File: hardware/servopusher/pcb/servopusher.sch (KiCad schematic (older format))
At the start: 1 part

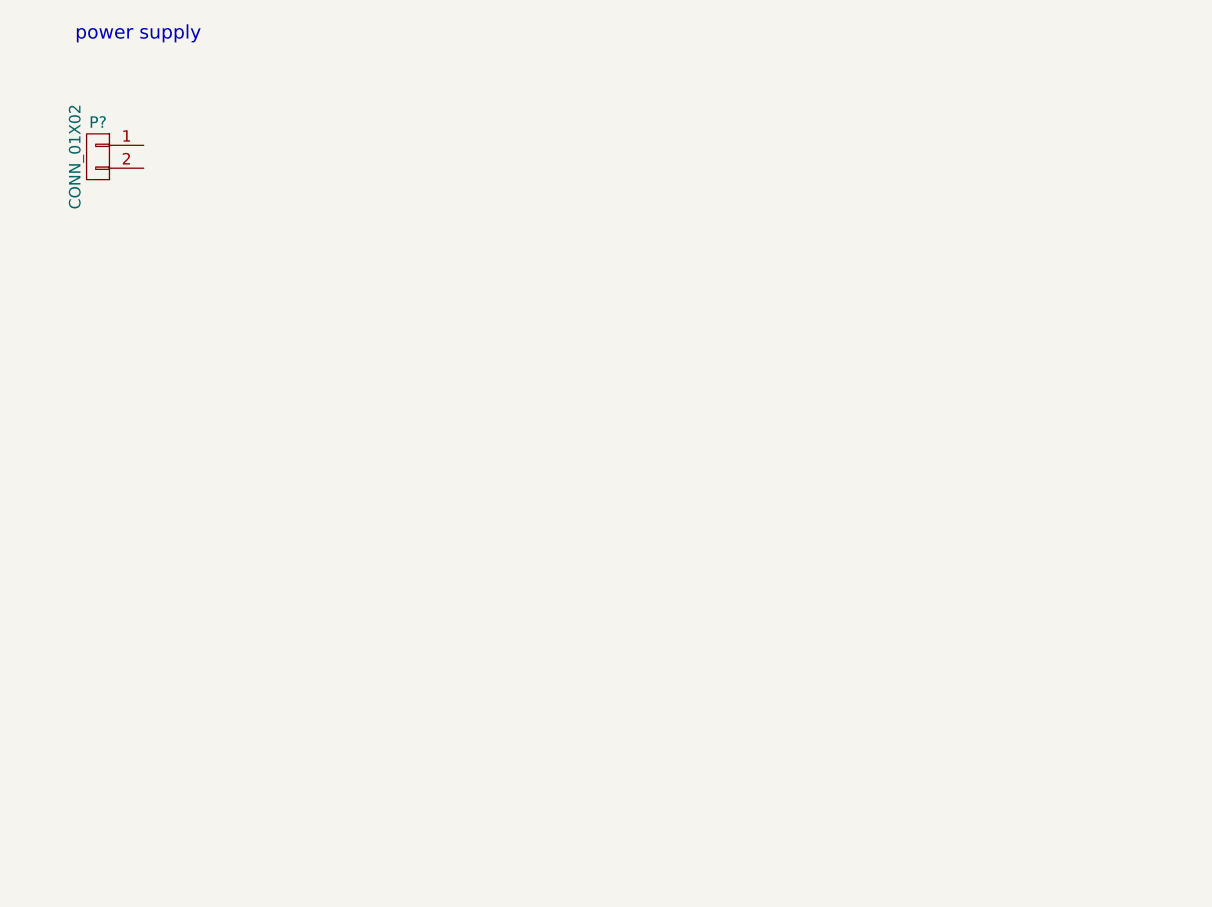
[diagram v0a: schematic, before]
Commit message: added attiny to schematic
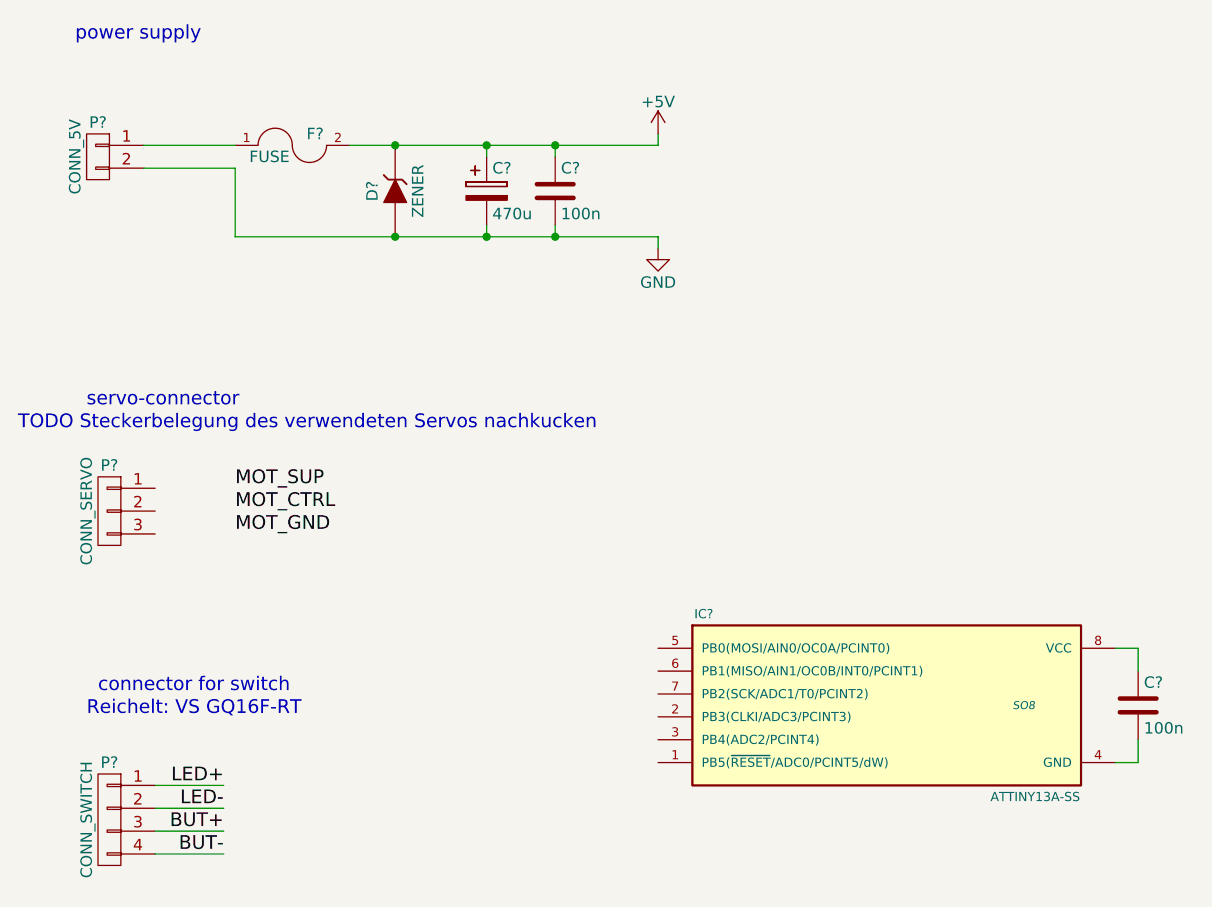
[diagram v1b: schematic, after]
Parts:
- added C?: 470u, symbol CP
- added C? (x2): 100n, symbol C
- added D?: ZENER, symbol ZENER
- added F?: FUSE, symbol FUSE
- added IC?: ATTINY13A-SS, SO8, symbol ATTINY13A-SS
- added P?: CONN_SERVO, symbol CONN_01X03
- added P?: CONN_SWITCH, symbol CONN_01X04
- P?: value CONN_01X02 -> CONN_5V
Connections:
- net at P?.1 (P1): now also F?.1
- net GND: now reaches P?.2 (P2)
- net GND: now also C?.2, C?.2, D?.1 (A)
- new net: C?.2, IC?.4 (GND)
- new net: C?.1, IC?.8 (VCC)
- new net +5V: C?.1, C?.1, D?.2 (K), F?.2
- new net BUT+: P?.3 (P3)
- new net BUT-: P?.4 (P4)
- new net LED+: P?.1 (P1)
- new net LED-: P?.2 (P2)
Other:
- note added: "Reichelt: VS GQ16F-RT"
- note added: "TODO Steckerbelegung des verwendeten Servos nachkucken"
- note added: "connector for switch"
- note added: "servo-connector"
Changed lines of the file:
@@
 LIBS:contrib
 LIBS:valves
+LIBS:servopusher-cache
 EELAYER 25 0
 EELAYER END
@@
 P 950 1300
 F 0 "P?" H 950 1450 50  0000 C CNN
-F 1 "CONN_01X02" V 1050 1300 50  0000 C CNN
+F 1 "CONN_5V" V 1050 1300 50  0000 C CNN
 F 2 "" H 950 1300 60  0000 C CNN
 F 3 "" H 950 1300 60  0000 C CNN
@@
 	-1   0    0    -1
 $EndComp
+$Comp
+L FUSE F?
+U 1 1 554878C8
+P 1800 1250
+F 0 "F?" H 1900 1300 50  0000 C CNN
+F 1 "FUSE" H 1700 1200 50  0000 C CNN
+F 2 "" H 1800 1250 60  0000 C CNN
+F 3 "" H 1800 1250 60  0000 C CNN
+	1    1800 1250
+	1    0    0    -1
+$EndComp
+Wire Wire Line
+	1150 1250 1550 1250
+$Comp
+L ZENER D?
+U 1 1 55487907
+P 2250 1450
+F 0 "D?" H 2250 1550 50  0000 C CNN
+F 1 "ZENER" H 2250 1350 50  0000 C CNN
+F 2 "" H 2250 1450 60  0000 C CNN
+F 3 "" H 2250 1450 60  0000 C CNN
+	1    2250 1450
+	0    -1   -1   0
+$EndComp
+Wire Wire Line
+	2050 1250 3400 1250
+$Comp
+L CP C?
+U 1 1 5548DEE8
+P 2650 1450
+F 0 "C?" H 2675 1550 50  0000 L CNN
+F 1 "470u" H 2675 1350 50  0000 L CNN
+F 2 "" H 2688 1300 30  0000 C CNN
+F 3 "" H 2650 1450 60  0000 C CNN
+	1    2650 1450
+	1    0    0    -1
+$EndComp
+$Comp
+L C C?
+U 1 1 5548DF2D
+P 2950 1450
+F 0 "C?" H 2975 1550 50  0000 L CNN
+F 1 "100n" H 2975 1350 50  0000 L CNN
+F 2 "" H 2988 1300 30  0000 C CNN
+F 3 "" H 2950 1450 60  0000 C CNN
+	1    2950 1450
+	1    0    0    -1
+$EndComp
+$Comp
+L GND #PWR?
+U 1 1 5548DFBB
+P 3400 1700
+F 0 "#PWR?" H 3400 1450 50  0001 C CNN
+F 1 "GND" H 3400 1550 50  0000 C CNN
+F 2 "" H 3400 1700 60  0000 C CNN
+F 3 "" H 3400 1700 60  0000 C CNN
+	1    3400 1700
+	1    0    0    -1
+$EndComp
+$Comp
+L +5V #PWR?
+U 1 1 5548DFCF
+P 3400 1200
+F 0 "#PWR?" H 3400 1050 50  0001 C CNN
+F 1 "+5V" H 3400 1340 50  0000 C CNN
+F 2 "" H 3400 1200 60  0000 C CNN
+F 3 "" H 3400 1200 60  0000 C CNN
+	1    3400 1200
+	1    0    0    -1
+$EndComp
+Wire Wire Line
+	3400 1250 3400 1200
+Connection ~ 2250 1250
+Wire Wire Line
+	3400 1650 3400 1700
+Wire Wire Line
+	2950 1600 2950 1650
+Connection ~ 2950 1650
+Wire Wire Line
+	2950 1300 2950 1250
+Connection ~ 2950 1250
+Wire Wire Line
+	2650 1300 2650 1250
+Connection ~ 2650 1250
+Wire Wire Line
+	2650 1600 2650 1650
+Connection ~ 2650 1650
+Wire Wire Line
+	1150 1350 1550 1350
+Connection ~ 2250 1650
+Wire Wire Line
+	1550 1350 1550 1650
+Wire Wire Line
+	1550 1650 3400 1650
+Text Notes 900  2400 0    60   ~ 0
+servo-connector
+$Comp
+L CONN_01X03 P?
+U 1 1 5548E134
+P 1000 2850
+F 0 "P?" H 1000 3050 50  0000 C CNN
+F 1 "CONN_SERVO" V 1100 2850 50  0000 C CNN
+F 2 "" H 1000 2850 60  0000 C CNN
+F 3 "" H 1000 2850 60  0000 C CNN
+	1    1000 2850
+	-1   0    0    -1
+$EndComp
+Text Notes 600  2500 0    60   ~ 0
+TODO Steckerbelegung des verwendeten Servos nachkucken
+Text Notes 950  3650 0    60   ~ 0
+connector for switch
+Text Notes 900  3750 0    60   ~ 0
+Reichelt: VS GQ16F-RT
+$Comp
+L CONN_01X04 P?
+U 1 1 5548E2EF
+P 1000 4200
+F 0 "P?" H 1000 4450 50  0000 C CNN
+F 1 "CONN_SWITCH" V 1100 4200 50  0000 C CNN
+F 2 "" H 1000 4200 60  0000 C CNN
+F 3 "" H 1000 4200 60  0000 C CNN
+	1    1000 4200
+	-1   0    0    -1
+$EndComp
+Text Label 1500 4050 2    60   ~ 0
+LED+
+Text Label 1500 4150 2    60   ~ 0
+LED-
+Text Label 1500 4250 2    60   ~ 0
+BUT+
+Text Label 1500 4350 2    60   ~ 0
+BUT-
+Wire Wire Line
+	1500 4050 1200 4050
+Wire Wire Line
+	1200 4150 1500 4150
+Wire Wire Line
+	1200 4250 1500 4250
+Wire Wire Line
+	1200 4350 1500 4350
+Text Label 1550 2750 0    60   ~ 0
+MOT_SUP
+Text Label 1550 2850 0    60   ~ 0
+MOT_CTRL
+Text Label 1550 2950 0    60   ~ 0
+MOT_GND
+$Comp
+L ATTINY13A-SS IC?
+U 1 1 557E11EB
+P 4400 3700
+F 0 "IC?" H 3600 4100 40  0000 C CNN
+F 1 "ATTINY13A-SS" H 5050 3300 40  0000 C CNN
+F 2 "SO8" H 5000 3700 35  0000 C CIN
+F 3 "" H 3600 4050 60  0000 C CNN
+	1    4400 3700
+	1    0    0    -1
+$EndComp
+$Comp
+L C C?
+U 1 1 557E123A
+P 5500 3700
+F 0 "C?" H 5525 3800 50  0000 L CNN
+F 1 "100n" H 5525 3600 50  0000 L CNN
+F 2 "" H 5538 3550 30  0000 C CNN
+F 3 "" H 5500 3700 60  0000 C CNN
+	1    5500 3700
+	1    0    0    -1
+$EndComp
+Wire Wire Line
+	5400 3450 5500 3450
+Wire Wire Line
+	5500 3450 5500 3550
+Wire Wire Line
+	5500 3850 5500 3950
+Wire Wire Line
+	5500 3950 5400 3950
 $EndSCHEMATC
